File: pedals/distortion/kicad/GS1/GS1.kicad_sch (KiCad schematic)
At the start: 22 parts, among them J1 AudioJack2, J2 AudioJack2, U1 LM741

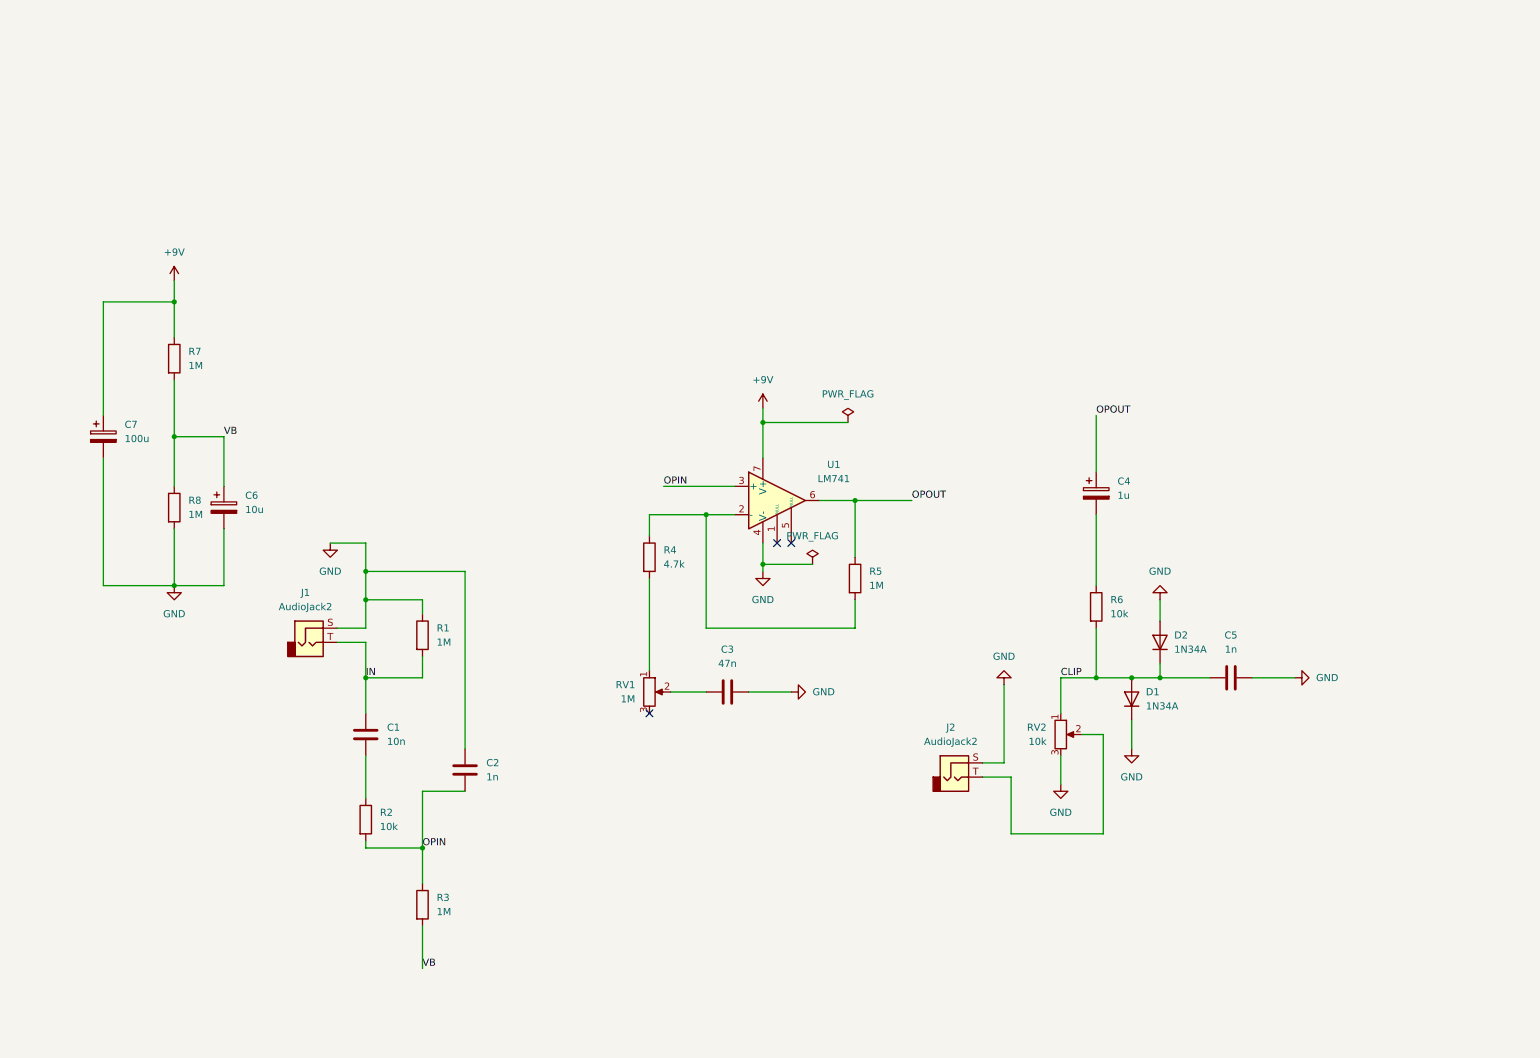
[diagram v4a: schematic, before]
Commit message: Add power input, true-bypass footswitch and LED to GS1
Adds a shared GreywireStudio symbol library with a 3PDT footswitch symbol.

Co-Authored-By: Claude Opus 5.5 <noreply@anthropic.com>
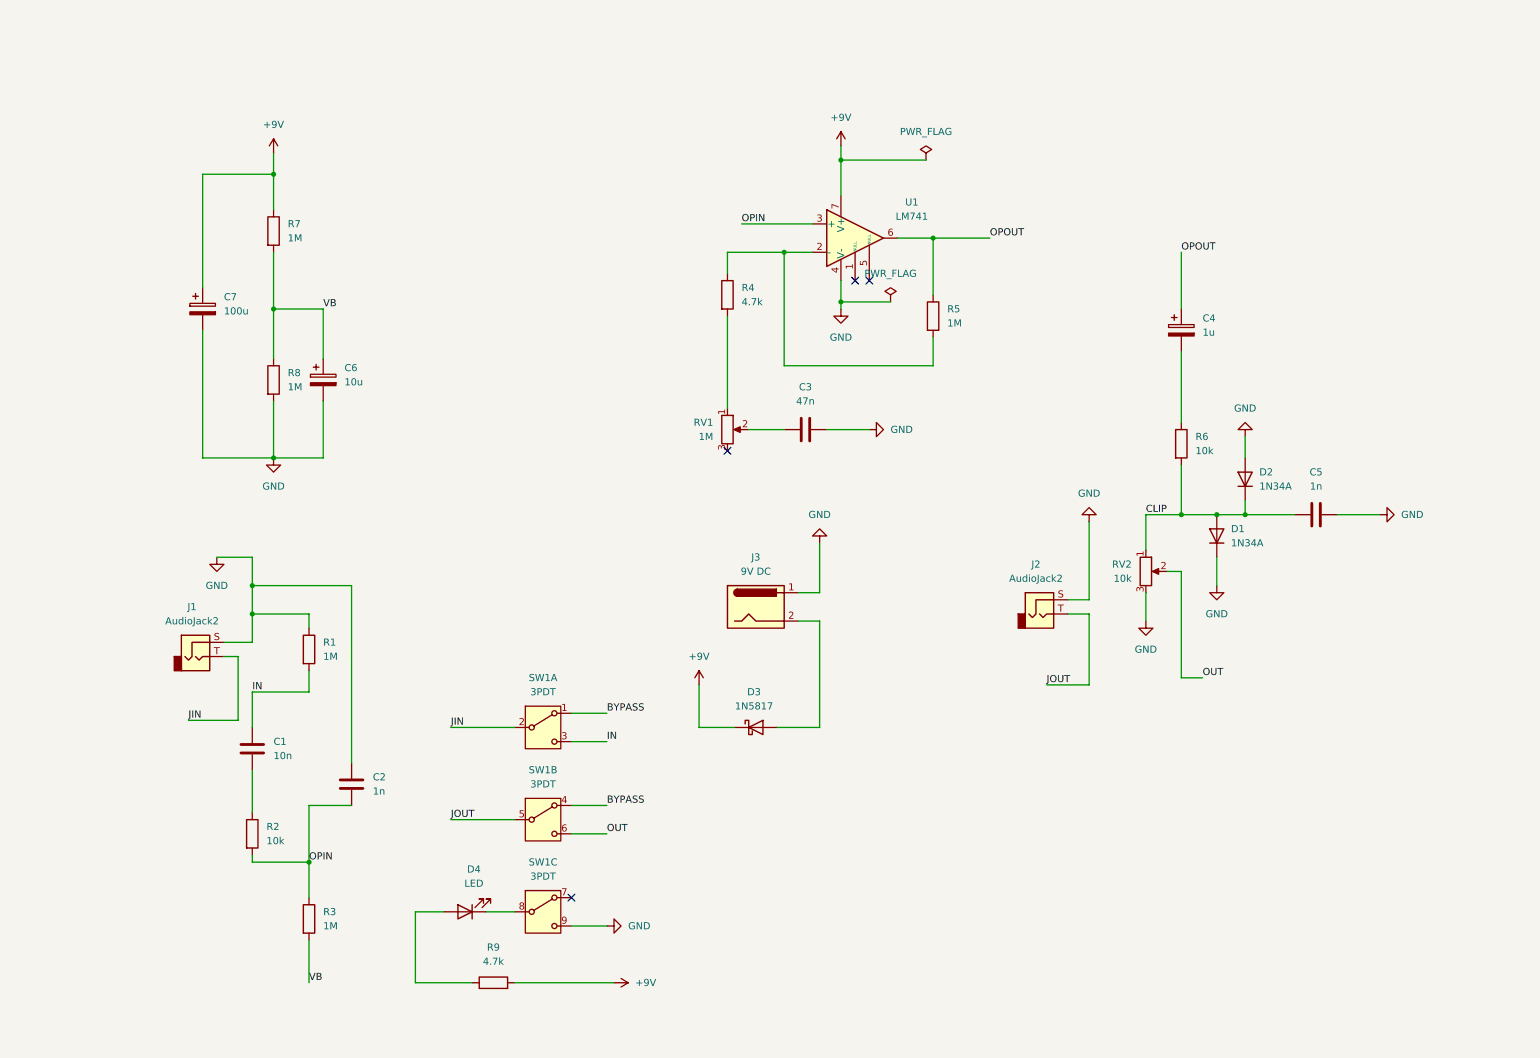
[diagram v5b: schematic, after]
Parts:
- added D3: 1N5817, symbol Device:D_Schottky
- added D4: LED, LED_SMD:LED_Cree-XHP50_3V_HighDensity, symbol Device:LED
- added J3: 9V DC, Package_DFN_QFN:Texas_RVA_VQFN-16-1EP_3.5x3.5mm_P0.5mm_EP2.14x2.14mm_ThermalVias, symbol Connector:Barrel_Jack
- added R9: 4.7k, LED_SMD:LED_Cree-XHP50_3V_HighDensity, symbol Device:R
- added SW1: 3PDT, Package_SO:SOIC-20W_7.5x12.8mm_P1.27mm, symbol GreywireStudio:SW_3PDT
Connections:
- net +9V: now also D3.1 (K), R9.2
- net GND: now also J3.1, SW1.9
- net IN: now also SW1.3; no longer J1.T
- net JOUT: now reaches J2.T
- net JOUT: now also SW1.5; no longer RV2.2
- new net: D4.2 (A), R9.1
- new net: D4.1 (K), SW1.8
- new net: D3.2 (A), J3.2
- new net BYPASS: SW1.1, SW1.4
- new net JIN: J1.T, SW1.2
- new net OUT: RV2.2, SW1.6
- no-connect marks 3 -> 4
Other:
- moved on the sheet: C1, C2, C3, C4, C5, C6, C7, D1, D2, J1, J2, R1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

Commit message: Add section headings and dividers to GS1 schematic
Co-Authored-By: Claude Opus 5.5 <noreply@anthropic.com>
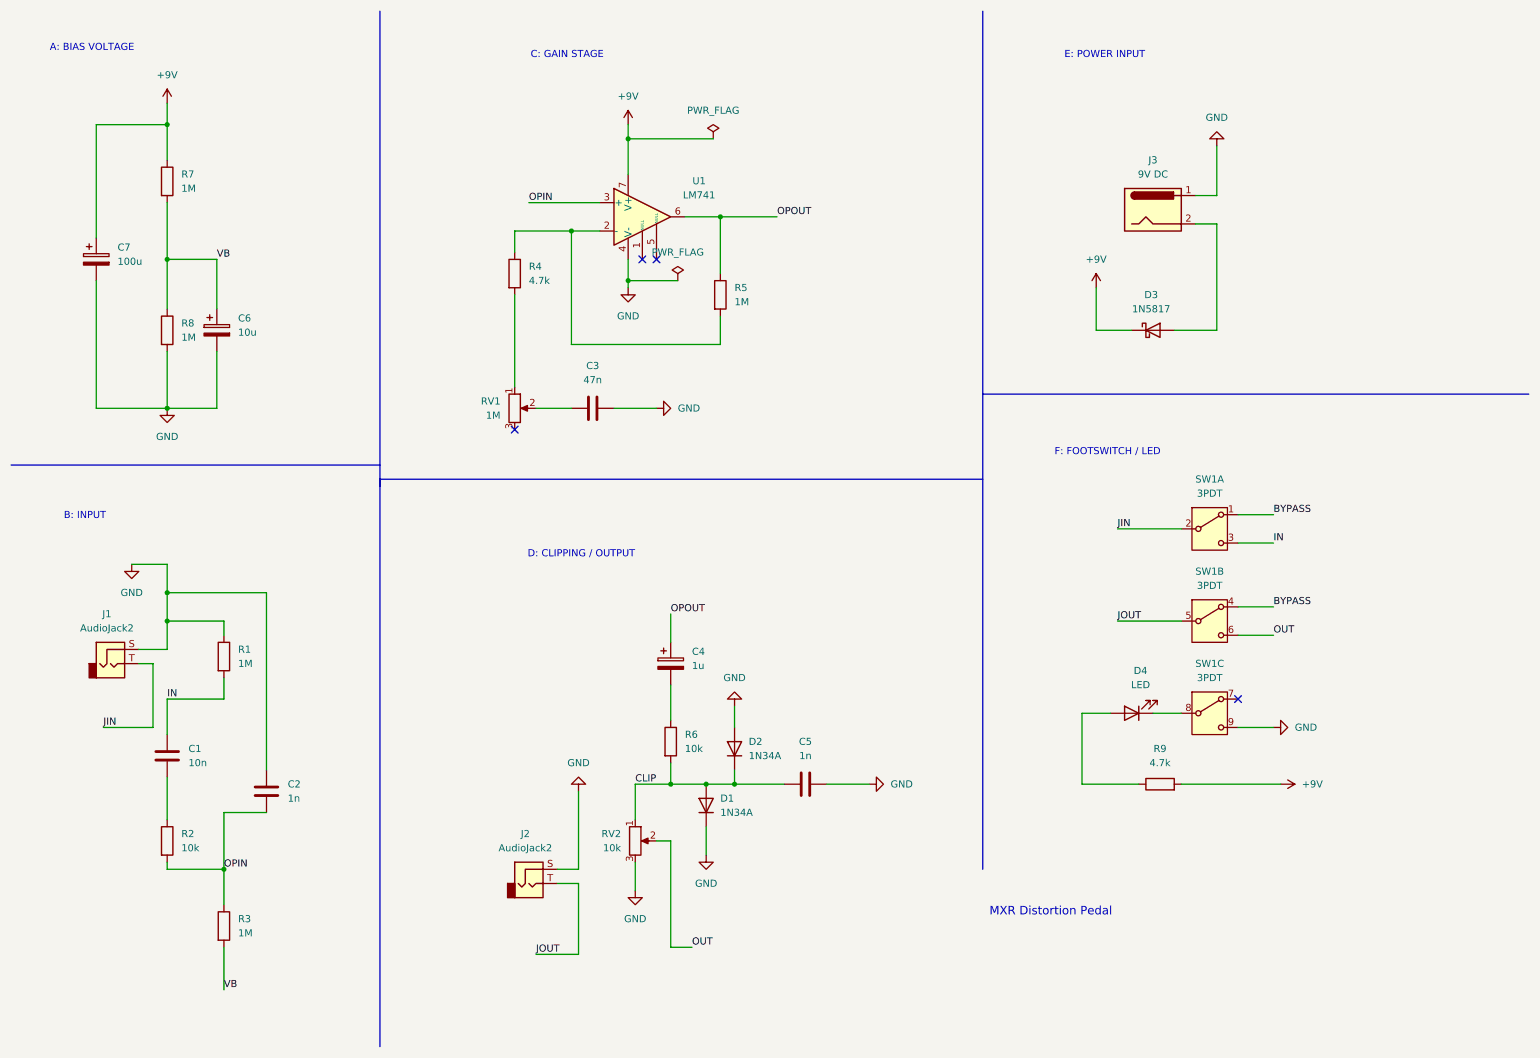
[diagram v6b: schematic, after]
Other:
- note added: "A: BIAS VOLTAGE"
- note added: "B: INPUT"
- note added: "C: GAIN STAGE"
- note added: "D: CLIPPING / OUTPUT"
- note added: "E: POWER INPUT"
- note added: "F: FOOTSWITCH / LED"
- note added: "MXR Distortion Pedal"
- moved on the sheet: C1, C2, C3, C4, C5, C6, C7, D1, D2, D3, D4, J1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

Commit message: Rename GS1 schematic title; remove stray divider segment
Co-Authored-By: Claude Opus 5.5 <noreply@anthropic.com>
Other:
- note added: "GS1 Distortion (based on MXR)"
- note removed: "MXR Distortion Pedal"
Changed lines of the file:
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@@
 	(generator_version "10.0")
 	(paper "A4")
-	(text "MXR Distortion Pedal"
+	(text "GS1 Distortion (based on MXR)"
 		(exclude_from_sim no)
 		(at 198.882 173.99 0)
@@
 		)
 	)
+	(polyline
+		(pts
+			(xy 78.74 12.7) (xy 78.74 198.12)
+		)
+		(stroke
+			(width 0)
+			(type default)
+		)
+	)
 	(wire
 		(pts
@@
 		)
 	)
+	(wire
+		(pts
+			(xy 120.65 83.82) (xy 128.27 83.82)
+		)
+		(stroke
+			(width 0)
+			(type default)
+		)
+	)
+	(wire
+		(pts
+			(xy 232.41 140.97) (xy 238.76 140.97)
+		)
+		(stroke
+			(width 0)
+			(type default)
+		)
+	)
+	(wire
+		(pts
+			(xy 40.64 73.66) (xy 40.64 83.82)
+		)
+		(stroke
+			(width 0)
+			(type default)
+		)
+	)
+	(wire
+		(pts
+			(xy 228.6 45.72) (xy 224.79 45.72)
+		)
+		(stroke
+			(width 0)
+			(type default)
+		)
+	)
+	(wire
+		(pts
+			(xy 123.19 35.56) (xy 123.19 41.91)
+		)
+		(stroke
+			(width 0)
+			(type default)
+		)
+	)
+	(wire
+		(pts
+			(xy 139.7 67.31) (xy 139.7 72.39)
+		)
+		(stroke
+			(width 0)
+			(type default)
+		)
+	)
+	(wire
+		(pts
+			(xy 228.6 50.8) (xy 228.6 69.85)
+		)
+		(stroke
+			(width 0)
+			(type default)
+		)
+	)
+	(wire
+		(pts
+			(xy 114.3 168.91) (xy 114.3 181.61)
+		)
+		(stroke
+			(width 0)
+			(type default)
+		)
+	)
+	(wire
+		(pts
+			(xy 40.64 116.84) (xy 40.64 121.92)
+		)
+		(stroke
+			(width 0)
+			(type default)
+		)
+	)
+	(wire
+		(pts
+			(xy 209.55 138.43) (xy 204.47 138.43)
+		)
+		(stroke
+			(width 0)
+			(type default)
+		)
+	)
+	(wire
+		(pts
+			(xy 204.47 138.43) (xy 204.47 151.13)
+		)
+		(stroke
+			(width 0)
+			(type default)
+		)
+	)
+	(wire
+		(pts
+			(xy 50.8 121.92) (xy 50.8 124.46)
+		)
+		(stroke
+			(width 0)
+			(type default)
+		)
+	)
+	(wire
+		(pts
+			(xy 113.03 52.07) (xy 118.11 52.07)
+		)
+		(stroke
+			(width 0)
+			(type default)
+		)
+	)
+	(wire
+		(pts
+			(xy 49.53 73.66) (xy 49.53 83.82)
+		)
+		(stroke
+			(width 0)
+			(type default)
+		)
+	)
+	(wire
+		(pts
+			(xy 232.41 107.95) (xy 238.76 107.95)
+		)
+		(stroke
+			(width 0)
+			(type default)
+		)
+	)
+	(wire
+		(pts
+			(xy 130.81 180.34) (xy 134.62 180.34)
+		)
+		(stroke
+			(width 0)
+			(type default)
+		)
+	)
+	(wire
+		(pts
+			(xy 158.75 151.13) (xy 166.37 151.13)
+		)
+		(stroke
+			(width 0)
+			(type default)
+		)
+	)
 	(polyline
 		(pts
-			(xy 78.74 12.7) (xy 78.74 198.12)
-		)
-		(stroke
-			(width 0)
-			(type default)
-		)
-	)
-	(wire
-		(pts
-			(xy 120.65 83.82) (xy 128.27 83.82)
-		)
-		(stroke
-			(width 0)
-			(type default)
-		)
-	)
-	(wire
-		(pts
-			(xy 232.41 140.97) (xy 238.76 140.97)
-		)
-		(stroke
-			(width 0)
-			(type default)
-		)
-	)
-	(wire
-		(pts
-			(xy 40.64 73.66) (xy 40.64 83.82)
-		)
-		(stroke
-			(width 0)
-			(type default)
-		)
-	)
-	(wire
-		(pts
-			(xy 228.6 45.72) (xy 224.79 45.72)
-		)
-		(stroke
-			(width 0)
-			(type default)
-		)
-	)
-	(wire
-		(pts
-			(xy 123.19 35.56) (xy 123.19 41.91)
-		)
-		(stroke
-			(width 0)
-			(type default)
-		)
-	)
-	(wire
-		(pts
-			(xy 139.7 67.31) (xy 139.7 72.39)
-		)
-		(stroke
-			(width 0)
-			(type default)
-		)
-	)
-	(wire
-		(pts
-			(xy 228.6 50.8) (xy 228.6 69.85)
-		)
-		(stroke
-			(width 0)
-			(type default)
-		)
-	)
-	(wire
-		(pts
-			(xy 114.3 168.91) (xy 114.3 181.61)
-		)
-		(stroke
-			(width 0)
-			(type default)
-		)
-	)
-	(wire
-		(pts
-			(xy 40.64 116.84) (xy 40.64 121.92)
-		)
-		(stroke
-			(width 0)
-			(type default)
-		)
-	)
-	(wire
-		(pts
-			(xy 209.55 138.43) (xy 204.47 138.43)
-		)
-		(stroke
-			(width 0)
-			(type default)
-		)
-	)
-	(wire
-		(pts
-			(xy 204.47 138.43) (xy 204.47 151.13)
-		)
-		(stroke
-			(width 0)
-			(type default)
-		)
-	)
-	(wire
-		(pts
-			(xy 50.8 121.92) (xy 50.8 124.46)
-		)
-		(stroke
-			(width 0)
-			(type default)
-		)
-	)
-	(wire
-		(pts
-			(xy 113.03 52.07) (xy 118.11 52.07)
-		)
-		(stroke
-			(width 0)
-			(type default)
-		)
-	)
-	(wire
-		(pts
-			(xy 49.53 73.66) (xy 49.53 83.82)
-		)
-		(stroke
-			(width 0)
-			(type default)
-		)
-	)
-	(wire
-		(pts
-			(xy 232.41 107.95) (xy 238.76 107.95)
-		)
-		(stroke
-			(width 0)
-			(type default)
-		)
-	)
-	(wire
-		(pts
-			(xy 130.81 180.34) (xy 134.62 180.34)
-		)
-		(stroke
-			(width 0)
-			(type default)
-		)
-	)
-	(wire
-		(pts
-			(xy 158.75 151.13) (xy 166.37 151.13)
-		)
-		(stroke
-			(width 0)
-			(type default)
-		)
-	)
-	(polyline
-		(pts
 			(xy 12.7 93.98) (xy 78.74 93.98)
 		)
@@
 		)
 		(stroke
-			(width 0)
-			(type default)
-		)
-	)
-	(polyline
-		(pts
-			(xy 78.74 96.52) (xy 78.74 97.79)
-		)
-		(stroke
